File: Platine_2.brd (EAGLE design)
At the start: 88.9 x 101.6 mm, 21 parts, among them X2 DTF13-12PA

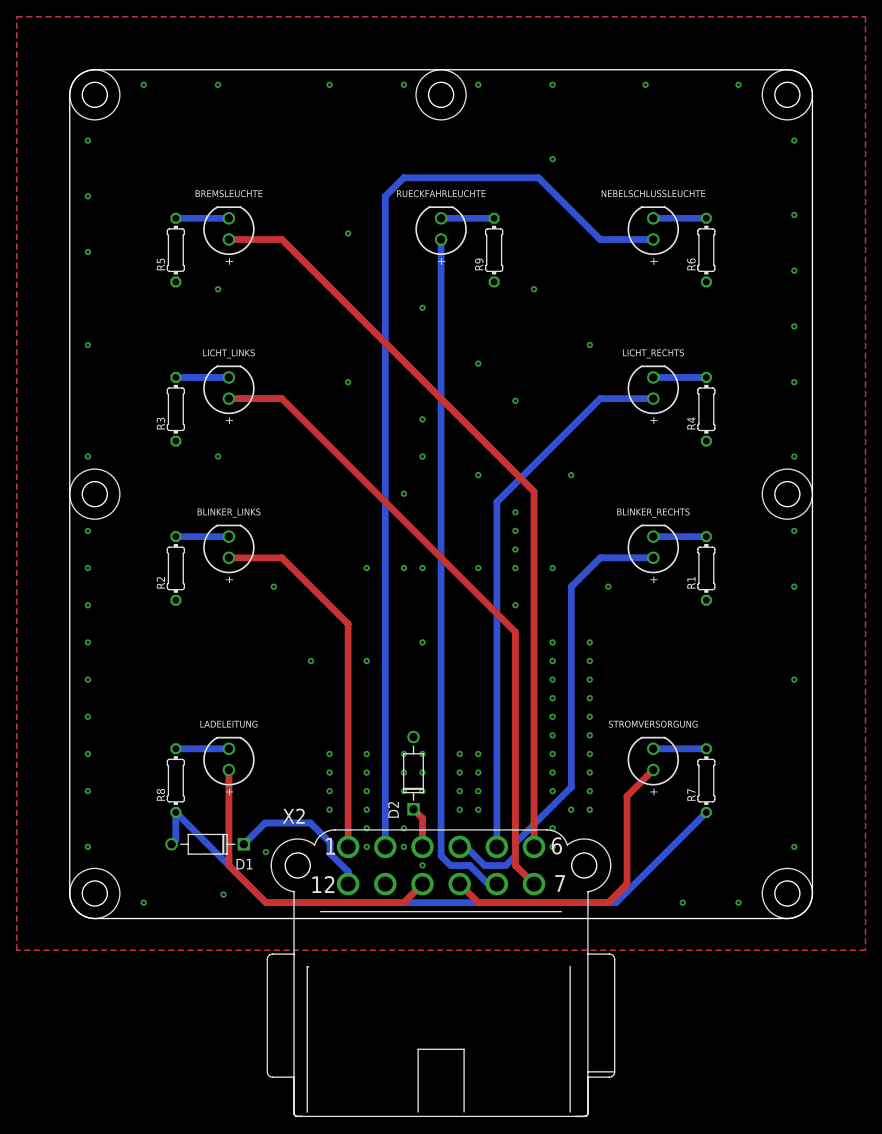
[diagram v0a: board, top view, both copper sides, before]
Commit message: bigger Resistors.
gitflow-feature-stash: better_solderable
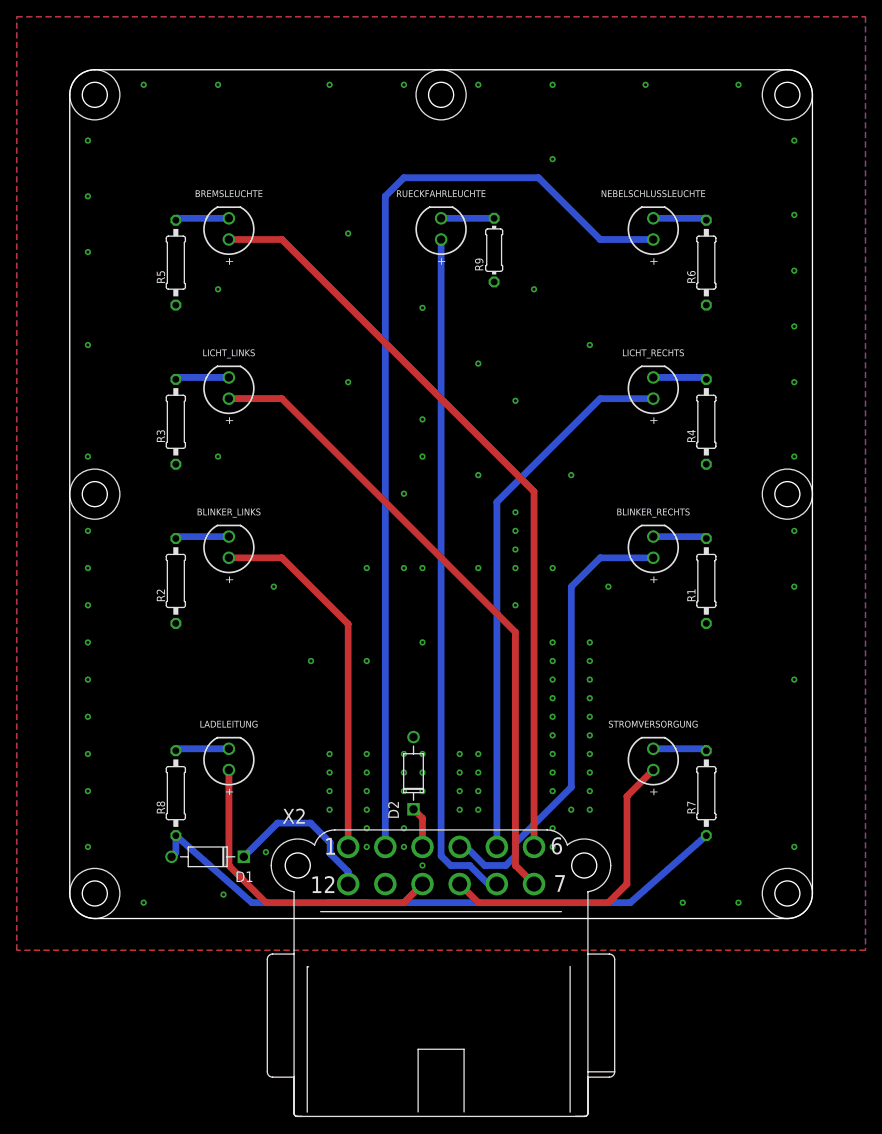
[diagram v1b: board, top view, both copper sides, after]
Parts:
- R1, R2, R3, R4, R5, R6, R7, R8: device resistor:0204/7 -> rcl:0207/10
- moved D1 1.50 mm to (-27.9, 1.04)
- moved R1 1.50 mm to (31.8, 34.1)
- moved R2 1.50 mm to (-31.8, 34.1)
- moved R3 1.50 mm to (-31.8, 53.1)
- moved R4 1.50 mm to (31.8, 53.1)
- moved R5 1.50 mm to (-31.8, 72.2)
- moved R6 1.50 mm to (31.8, 72.2)
- moved R7 1.50 mm to (31.8, 8.66)
- moved R8 1.50 mm to (-31.8, 8.66)
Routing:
- net MASSE_9: track 76.5 -> 72.3 mm
- net N$10: track 18.2 -> 18.8 mm

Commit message: should be better solderable.
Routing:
- net MASSE_9: track 72.3 -> 72.9 mm
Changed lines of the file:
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@@
 <param name="msMicroVia" value="9.99mm"/>
 <param name="msBlindViaRatio" value="0.5"/>
-<param name="rvPadTop" value="0.25"/>
-<param name="rvPadInner" value="0.25"/>
-<param name="rvPadBottom" value="0.25"/>
+<param name="rvPadTop" value="0.4"/>
+<param name="rvPadInner" value="0.4"/>
+<param name="rvPadBottom" value="0.4"/>
 <param name="rvViaOuter" value="0.25"/>
 <param name="rvViaInner" value="0.25"/>
 <param name="rvMicroViaOuter" value="0.25"/>
 <param name="rvMicroViaInner" value="0.25"/>
-<param name="rlMinPadTop" value="10mil"/>
-<param name="rlMaxPadTop" value="20mil"/>
-<param name="rlMinPadInner" value="10mil"/>
-<param name="rlMaxPadInner" value="20mil"/>
-<param name="rlMinPadBottom" value="10mil"/>
-<param name="rlMaxPadBottom" value="20mil"/>
+<param name="rlMinPadTop" value="20mil"/>
+<param name="rlMaxPadTop" value="50mil"/>
+<param name="rlMinPadInner" value="20mil"/>
+<param name="rlMaxPadInner" value="50mil"/>
+<param name="rlMinPadBottom" value="20mil"/>
+<param name="rlMaxPadBottom" value="50mil"/>
 <param name="rlMinViaOuter" value="8mil"/>
 <param name="rlMaxViaOuter" value="20mil"/>
@@
 <param name="checkFont" value="1"/>
 <param name="checkRestrict" value="1"/>
-<param name="checkStop" value="1"/>
+<param name="checkStop" value="0"/>
 <param name="checkValues" value="1"/>
 <param name="checkNames" value="1"/>
@@
 <wire x1="5.212" y1="0" x2="7.747" y2="0" width="0.8128" layer="16"/>
 <wire x1="7.747" y1="0" x2="8.9" y2="1.153" width="0.8128" layer="16"/>
-<wire x1="8.9" y1="1.153" x2="8.9" y2="2.69695625" width="0.8128" layer="16"/>
-<wire x1="15.585" y1="9.38195625" x2="15.585" y2="33.365" width="0.8128" layer="16"/>
-<wire x1="8.9" y1="2.69695625" x2="15.585" y2="9.38195625" width="0.8128" layer="16"/>
+<wire x1="8.9" y1="1.153" x2="8.9" y2="3.20495625" width="0.8128" layer="16"/>
+<wire x1="15.585" y1="9.88995625" x2="15.585" y2="33.365" width="0.8128" layer="16"/>
+<wire x1="8.9" y1="3.20495625" x2="15.585" y2="9.88995625" width="0.8128" layer="16"/>
 </signal>
 <signal name="STROMVERSORGUNG_9">
@@
 <via x="17.8" y="26.7" extent="1-16" drill="0.35"/>
 <via x="13.35" y="11.125" extent="1-16" drill="0.35"/>
-<via x="13.35" y="8.9" extent="1-16" drill="0.35"/>
+<via x="13.35" y="9.281" extent="1-16" drill="0.35"/>
 <via x="4.45" y="8.9" extent="1-16" drill="0.35"/>
 <via x="4.45" y="6.675" extent="1-16" drill="0.35"/>
@@
 <contactref element="BLINKER_LINKS" pad="1"/>
 <contactref element="R2" pad="2"/>
-<wire x1="-31.704" y1="39.37" x2="-25.4" y2="39.37" width="0.8128" layer="16"/>
-<wire x1="-31.704" y1="39.37" x2="-31.75" y2="39.14" width="0.8128" layer="16"/>
+<wire x1="-31.75" y1="39.14" x2="-31.52" y2="39.37" width="0.8128" layer="16"/>
+<wire x1="-31.52" y1="39.37" x2="-25.4" y2="39.37" width="0.8128" layer="16"/>
 </signal>
 <signal name="N$5">
 <contactref element="BLINKER_RECHTS" pad="1"/>
 <contactref element="R1" pad="2"/>
-<wire x1="31.75" y1="39.14" x2="31.704" y2="39.37" width="0.8128" layer="16"/>
-<wire x1="25.4" y1="39.37" x2="31.704" y2="39.37" width="0.8128" layer="16"/>
+<wire x1="31.75" y1="39.14" x2="31.52" y2="39.37" width="0.8128" layer="16"/>
+<wire x1="31.52" y1="39.37" x2="25.4" y2="39.37" width="0.8128" layer="16"/>
 </signal>
 <signal name="N$1">
 <contactref element="R3" pad="2"/>
 <contactref element="LICHT_LINKS" pad="1"/>
-<wire x1="-25.4" y1="58.42" x2="-31.704" y2="58.42" width="0.8128" layer="16"/>
-<wire x1="-31.704" y1="58.42" x2="-31.75" y2="58.19" width="0.8128" layer="16"/>
+<wire x1="-31.75" y1="58.19" x2="-31.52" y2="58.42" width="0.8128" layer="16"/>
+<wire x1="-31.52" y1="58.42" x2="-25.4" y2="58.42" width="0.8128" layer="16"/>
 </signal>
 <signal name="N$2">
 <contactref element="R4" pad="2"/>
 <contactref element="LICHT_RECHTS" pad="1"/>
-<wire x1="31.75" y1="58.19" x2="31.704" y2="58.42" width="0.8128" layer="16"/>
-<wire x1="25.4" y1="58.42" x2="31.704" y2="58.42" width="0.8128" layer="16"/>
+<wire x1="31.75" y1="58.19" x2="31.52" y2="58.42" width="0.8128" layer="16"/>
+<wire x1="31.52" y1="58.42" x2="25.4" y2="58.42" width="0.8128" layer="16"/>
 </signal>
 <signal name="N$4">
 <contactref element="R5" pad="2"/>
 <contactref element="BREMSLEUCHTE" pad="1"/>
-<wire x1="-25.4" y1="77.47" x2="-31.704" y2="77.47" width="0.8128" layer="16"/>
-<wire x1="-31.704" y1="77.47" x2="-31.75" y2="77.24" width="0.8128" layer="16"/>
+<wire x1="-31.75" y1="77.24" x2="-31.52" y2="77.47" width="0.8128" layer="16"/>
+<wire x1="-31.52" y1="77.47" x2="-25.4" y2="77.47" width="0.8128" layer="16"/>
 </signal>
 <signal name="N$6">
 <contactref element="R6" pad="2"/>
 <contactref element="NEBELSCHLUSSLEUCHTE" pad="1"/>
-<wire x1="31.75" y1="77.24" x2="31.704" y2="77.47" width="0.8128" layer="16"/>
-<wire x1="25.4" y1="77.47" x2="31.704" y2="77.47" width="0.8128" layer="16"/>
+<wire x1="31.75" y1="77.24" x2="31.52" y2="77.47" width="0.8128" layer="16"/>
+<wire x1="31.52" y1="77.47" x2="25.4" y2="77.47" width="0.8128" layer="16"/>
 </signal>
 <signal name="N$7">
 <contactref element="R7" pad="2"/>
 <contactref element="STROMVERSORGUNG" pad="1"/>
-<wire x1="31.75" y1="13.74" x2="31.704" y2="13.97" width="0.8128" layer="16"/>
-<wire x1="25.4" y1="13.97" x2="31.704" y2="13.97" width="0.8128" layer="16"/>
+<wire x1="31.75" y1="13.74" x2="31.52" y2="13.97" width="0.8128" layer="16"/>
+<wire x1="31.52" y1="13.97" x2="25.4" y2="13.97" width="0.8128" layer="16"/>
 </signal>
 <signal name="N$8">
 <contactref element="R8" pad="2"/>
 <contactref element="LADELEITUNG" pad="1"/>
-<wire x1="-31.704" y1="13.97" x2="-25.4" y2="13.97" width="0.8128" layer="16"/>
-<wire x1="-31.704" y1="13.97" x2="-31.75" y2="13.74" width="0.8128" layer="16"/>
+<wire x1="-31.75" y1="13.74" x2="-31.52" y2="13.97" width="0.8128" layer="16"/>
+<wire x1="-31.52" y1="13.97" x2="-25.4" y2="13.97" width="0.8128" layer="16"/>
 </signal>
 <signal name="N$9">
@@
 <contactref element="R7" pad="1"/>
 <contactref element="R8" pad="1"/>
-<wire x1="-8.9" y1="-4.4475" x2="-8.9" y2="-4.45" width="0.8128" layer="16"/>
-<wire x1="22.64989375" y1="-4.45" x2="31.75" y2="3.58" width="0.8128" layer="16"/>
-<wire x1="-8.9" y1="-4.45" x2="22.64989375" y2="-4.45" width="0.8128" layer="16"/>
-<wire x1="-13.35" y1="-4.45" x2="-13.35" y2="-4.4475" width="0.8128" layer="16"/>
-<wire x1="-22.64989375" y1="-4.45" x2="-31.75" y2="3.58" width="0.8128" layer="16"/>
-<wire x1="-13.35" y1="-4.45" x2="-22.64989375" y2="-4.45" width="0.8128" layer="16"/>
+<wire x1="-13.35" y1="-4.4475" x2="-13.35" y2="-4.45" width="0.8128" layer="16"/>
 <contactref element="D1" pad="A"/>
 <wire x1="-31.75" y1="3.58" x2="-31.75" y2="1.555" width="0.8128" layer="16"/>
@@
 <wire x1="-13.35" y1="-4.4475" x2="-8.9025" y2="-4.4475" width="0.8128" layer="16"/>
 <wire x1="-8.9025" y1="-4.4475" x2="-8.9" y2="-4.45" width="0.8128" layer="16"/>
+<wire x1="23.72" y1="-4.45" x2="31.75" y2="3.58" width="0.8128" layer="16"/>
+<wire x1="-8.9" y1="-4.45" x2="23.72" y2="-4.45" width="0.8128" layer="16"/>
+<wire x1="-23.72" y1="-4.45" x2="-31.75" y2="3.58" width="0.8128" layer="16"/>
+<wire x1="-13.35" y1="-4.45" x2="-23.72" y2="-4.45" width="0.8128" layer="16"/>
 </signal>
 <signal name="N$10">
@@
 <wire x1="-23.615" y1="1.04" x2="-19.575" y2="5.08" width="0.8128" layer="16"/>
 <wire x1="-19.575" y1="5.08" x2="-15.621" y2="5.08" width="0.8128" layer="16"/>
-<wire x1="-15.621" y1="5.08" x2="-13.2878" y2="2.7468" width="0.8128" layer="16"/>
-<wire x1="-13.2878" y1="2.7468" x2="-13.2878" y2="1.43184375" width="0.8128" layer="16"/>
-<wire x1="-11.125" y1="-0.73095625" x2="-11.125" y2="-2.2225" width="0.8128" layer="16"/>
-<wire x1="-13.2878" y1="1.43184375" x2="-11.125" y2="-0.73095625" width="0.8128" layer="16"/>
+<wire x1="-15.621" y1="5.08" x2="-13.373" y2="2.832" width="0.8128" layer="16"/>
+<wire x1="-13.373" y1="2.832" x2="-13.373" y2="0.992" width="0.8128" layer="16"/>
+<wire x1="-11.125" y1="-1.256" x2="-11.125" y2="-2.2225" width="0.8128" layer="16"/>
+<wire x1="-13.373" y1="0.992" x2="-11.125" y2="-1.256" width="0.8128" layer="16"/>
 </signal>
 <signal name="N$11">
